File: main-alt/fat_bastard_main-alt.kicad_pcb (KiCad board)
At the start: 2 copper layers, 195 x 50 mm, 60 parts, among them J1 INPUT, J2 TO_LD_12V, J3 TO_LD_IN, J4 TO_LD_GAIN, J5 TO_LD_OUT, J6 12V_IN, J8 FOOTSW, J9 OUTPUT, K1 FINDER-30.22, U1 OPA2134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

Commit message: Fix potentiometers orientation
Signed-off-by: Arnaud Ferraris <arnaud.ferraris@gmail.com>
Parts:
- removed JP1: Jumper, Jumper:SolderJumper-2_P1.3mm_Open_TrianglePad1.0x1.5mm
- C12: value 4.7n -> 10n
- R10: value 82k -> 33k
- R13: value 100k -> 47k
- R14: value 910k -> 1M
- R20: value 4.7k -> 3.3k
- R9: value 3.9k -> 2.2k
- REF**: value OSHW-Logo2_7.3x6mm_SilkScreen -> OSHW-Logo2_14.6x12mm_SilkScreen; footprint Symbol:OSHW-Logo2_7.3x6mm_SilkScreen -> Symbol:OSHW-Logo2_14.6x12mm_SilkScreen
- moved C1 24.9 mm to (151.2, 108.5), turned to 90 degrees
- moved R5 22.5 mm to (96.0, 95.3), turned to 270 degrees
- moved C3 20.9 mm to (72.4, 108.1)
- moved C4 15.2 mm to (89.0, 92.2), turned to 270 degrees
- moved R4 11.4 mm to (85.1, 92.2), turned to 180 degrees
- moved R3 8.03 mm to (157.2, 89.0), turned to 0 degrees
- moved C10 5.03 mm to (100.1, 91.0)
- moved R2 4.22 mm to (151.2, 87.9), turned to 270 degrees
- moved C2 2.54 mm to (161.7, 94.7), turned to 0 degrees
- moved C6 2.52 mm to (137.7, 96.2), turned to 0 degrees
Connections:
- J4 pad 1: Net-(C6-Pad2) -> /LD_GND
- J4 pad 3: /LD_GND -> Net-(C6-Pad2)
- K1 pad 21: /LD_GND -> /LD_SIG
- K1 pad 22: /LD_SIG -> /LD_GND
- RV1 pad 1: Net-(C6-Pad2) -> /LD_GND
- RV1 pad 3: /LD_GND -> Net-(C6-Pad2)
- RV2 pad 1: Net-(C2-Pad2) -> Net-(C1-Pad2)
- RV2 pad 3: Net-(C1-Pad2) -> Net-(C2-Pad2)
- RV3 pad 1: Net-(RV3-Pad1) -> GNDS
- RV3 pad 3: GNDS -> Net-(RV3-Pad3)
- RV5 pad 1: Net-(C4-Pad2) -> Net-(C3-Pad2)
- RV5 pad 3: Net-(C3-Pad2) -> Net-(C4-Pad2)
- RV6 pad 1: Net-(RV5-Pad2) -> GNDS
- RV6 pad 3: GNDS -> Net-(RV5-Pad2)
- RV7 pad 1: Net-(C12-Pad2) -> GNDS
- RV7 pad 3: GNDS -> Net-(C12-Pad2)
- U1 pad 1: Net-(RV3-Pad1) -> Net-(RV3-Pad3)
- U1 pad 2: Net-(RV3-Pad1) -> Net-(RV3-Pad3)
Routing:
- net GNDS: track 241.6 -> 306.0 mm
- net Net-(RV3-Pad3): track 0.00 -> 35.6 mm
- net Net-(RV3-Pad1): track 26.6 -> 0.00 mm
- net Net-(R7-Pad1): track 48.1 -> 30.3 mm
- net Net-(C1-Pad2): track 24.8 -> 11.0 mm
- net Net-(RV5-Pad2): track 23.5 -> 34.4 mm
- net Net-(K1-Pad12): track 68.1 -> 59.1 mm, vias 0 -> 1
- net Net-(C2-Pad2): track 19.1 -> 26.2 mm
- net Net-(C4-Pad1): track 24.7 -> 18.0 mm
- net Net-(C15-Pad2): track 50.8 -> 45.0 mm
- net Net-(C3-Pad2): track 23.5 -> 18.9 mm
- net +12V: track 171.3 -> 175.3 mm
- net VCC: track 169.0 -> 172.2 mm
- net Net-(R14-Pad1): track 18.6 -> 17.6 mm, vias 1 -> 0
- net Net-(C6-Pad2): track 18.4 -> 17.6 mm
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
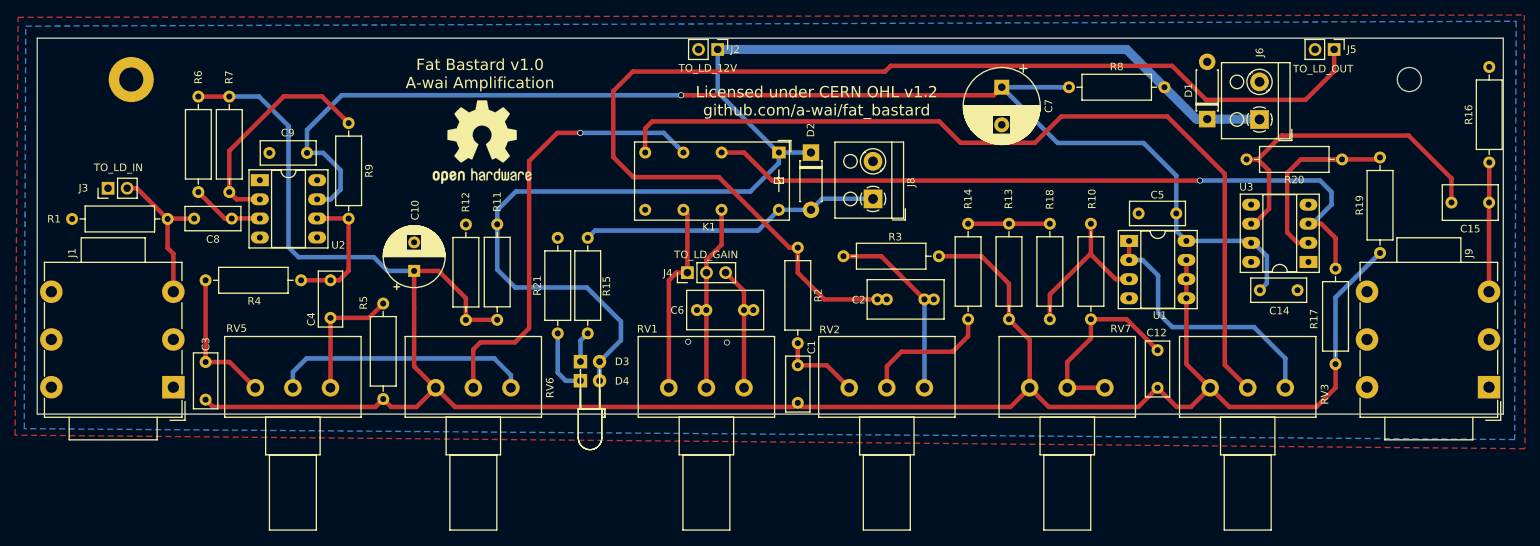
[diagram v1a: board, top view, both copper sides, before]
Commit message: Improve rounting
Signed-off-by: Arnaud Ferraris <arnaud.ferraris@gmail.com>
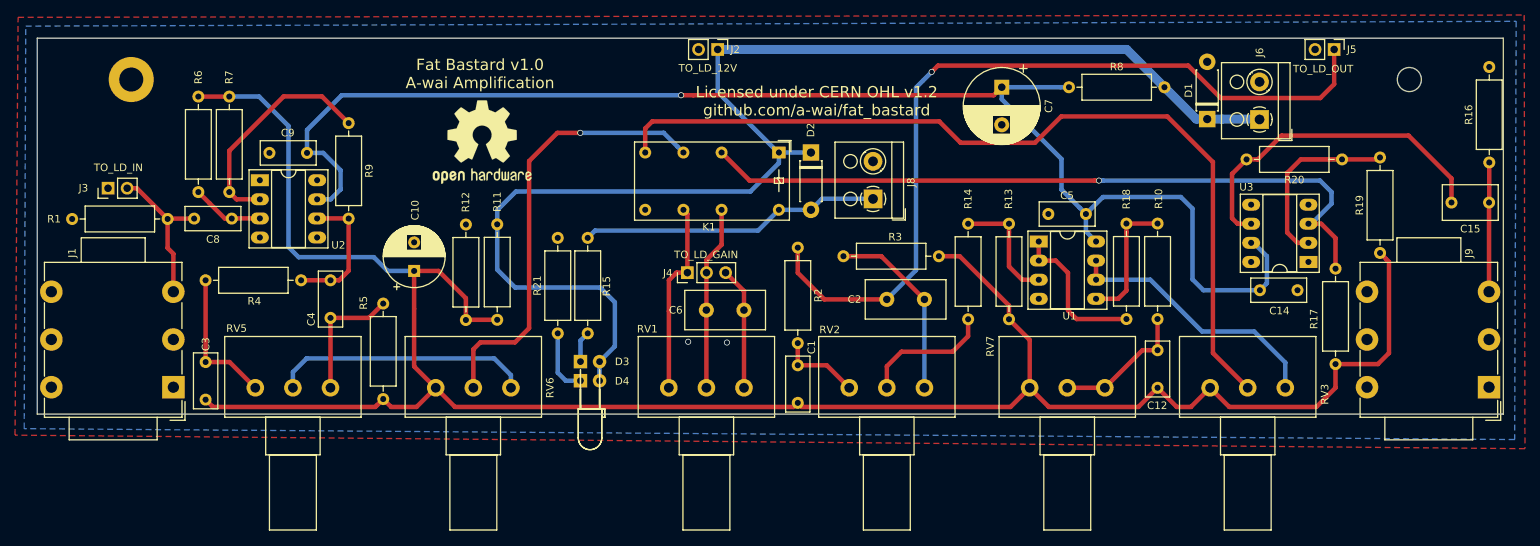
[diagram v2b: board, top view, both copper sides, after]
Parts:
- C2, C6: footprint Capacitor_THT:C_Rect_L10.0mm_W5.0mm_P5.00mm_P7.50mm -> Capacitor_THT:C_Disc_D10.5mm_W5.0mm_P5.00mm
- R1: value 1M -> 2.2M
- moved R18 16.3 mm to (194.9, 97.4), turned to 90 degrees
- moved U1 12.0 mm to (183.2, 87.0)
- moved C5 12.0 mm to (189.5, 83.4)
- moved R10 8.86 mm to (199.0, 84.7)
- moved C2 1.25 mm to (163.0, 94.7)
- moved C6 1.25 mm to (139.0, 96.2)
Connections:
- R18 pad 1: Net-(R13-Pad1) -> Net-(R18-Pad1)
- U1 pad 1: Net-(RV3-Pad3) -> Net-(R18-Pad1)
- U1 pad 2: Net-(RV3-Pad3) -> Net-(R18-Pad1)
- U1 pad 3: Net-(R10-Pad1) -> Net-(R13-Pad1)
- U1 pad 5: GNDS -> Net-(R10-Pad1)
- U1 pad 6: GNDS -> Net-(RV3-Pad3)
- U1 pad 7: GNDS -> Net-(RV3-Pad3)
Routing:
- net Net-(C2-Pad1): track 158.6 -> 110.4 mm, vias 0 -> 1
- net Net-(R18-Pad1): track 0.00 -> 20.3 mm
- net GNDS: track 306.0 -> 290.3 mm
- net VCC: track 172.2 -> 186.6 mm
- net Net-(C12-Pad2): track 26.0 -> 18.2 mm
- net Net-(R13-Pad1): track 10.9 -> 15.8 mm
- net Net-(R10-Pad1): track 21.5 -> 17.5 mm
- net Net-(C6-Pad2): track 17.6 -> 16.3 mm
- net Net-(C2-Pad2): track 26.2 -> 24.9 mm
- net /LD_SIG: track 25.8 -> 24.5 mm
- net Net-(C15-Pad2): track 45.0 -> 45.6 mm
